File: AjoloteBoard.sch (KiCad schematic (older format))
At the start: 4 parts, among them SW1 SW_Push_SPDT

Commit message: Update project to kicad 5
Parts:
- removed SW1: SW_Push_SPDT, Switches:MSK12C02, symbol SW_Push_SPDT
- added SW?: SW_DPDT_x2, symbol Switch:SW_DPDT_x2
- BT1: symbol Battery_Cell -> Device:Battery_Cell
- D1, D2: symbol LED -> Device:LED
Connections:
- wire segments 9 -> 11
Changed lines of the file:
@@
-EESchema Schematic File Version 2
-LIBS:power
-LIBS:device
-LIBS:transistors
-LIBS:conn
-LIBS:linear
-LIBS:regul
-LIBS:74xx
-LIBS:cmos4000
-LIBS:adc-dac
-LIBS:memory
-LIBS:xilinx
-LIBS:microcontrollers
-LIBS:dsp
-LIBS:microchip
-LIBS:analog_switches
-LIBS:motorola
-LIBS:texas
-LIBS:intel
-LIBS:audio
-LIBS:interface
-LIBS:digital-audio
-LIBS:philips
-LIBS:display
-LIBS:cypress
-LIBS:siliconi
-LIBS:opto
-LIBS:atmel
-LIBS:contrib
-LIBS:valves
-LIBS:74xgxx
-LIBS:ac-dc
-LIBS:actel
-LIBS:allegro
-LIBS:Altera
-LIBS:analog_devices
-LIBS:battery_management
-LIBS:bbd
-LIBS:bosch
-LIBS:brooktre
-LIBS:cmos_ieee
-LIBS:dc-dc
-LIBS:diode
-LIBS:elec-unifil
-LIBS:ESD_Protection
-LIBS:ftdi
-LIBS:gennum
-LIBS:graphic
-LIBS:hc11
-LIBS:ir
-LIBS:Lattice
-LIBS:logo
-LIBS:maxim
-LIBS:mechanical
-LIBS:microchip_dspic33dsc
-LIBS:microchip_pic10mcu
-LIBS:microchip_pic12mcu
-LIBS:microchip_pic16mcu
-LIBS:microchip_pic18mcu
-LIBS:microchip_pic32mcu
-LIBS:motor_drivers
-LIBS:motors
-LIBS:msp430
-LIBS:nordicsemi
-LIBS:nxp_armmcu
-LIBS:onsemi
-LIBS:Oscillators
-LIBS:Power_Management
-LIBS:powerint
-LIBS:pspice
-LIBS:references
-LIBS:relays
-LIBS:rfcom
-LIBS:sensors
-LIBS:silabs
-LIBS:stm8
-LIBS:stm32
-LIBS:supertex
-LIBS:switches
-LIBS:transf
-LIBS:ttl_ieee
-LIBS:video
-LIBS:wiznet
-LIBS:Worldsemi
-LIBS:Xicor
-LIBS:zetex
-LIBS:Zilog
+EESchema Schematic File Version 4
 LIBS:AjoloteBoard-cache
-EELAYER 25 0
+EELAYER 29 0
 EELAYER END
 $Descr A4 11693 8268
@@
 $EndDescr
 $Comp
-L LED D1
+L Device:LED D1
 U 1 1 5AF7924C
 P 4745 3090
@@
 $EndComp
 $Comp
-L LED D2
+L Device:LED D2
 U 1 1 5AF7929C
 P 5100 3120
@@
 $EndComp
 $Comp
-L Battery_Cell BT1
+L Device:Battery_Cell BT1
 U 1 1 5AF792E6
 P 3895 3190
@@
 	1    0    0    -1
 $EndComp
-$Comp
-L SW_Push_SPDT SW1
-U 1 1 5B1026CD
-P 4335 3375
-F 0 "SW1" H 4335 3545 50  0000 C CNN
-F 1 "SW_Push_SPDT" H 4335 3175 50  0000 C CNN
-F 2 "Switches:MSK12C02" H 4335 3375 50  0001 C CNN
-F 3 "" H 4335 3375 50  0000 C CNN
-	1    4335 3375
-	1    0    0    -1
-$EndComp
 Wire Wire Line
 	3895 2990 3895 2890
 Wire Wire Line
-	3895 2890 5100 2890
+	3895 2890 4745 2890
 Wire Wire Line
 	3895 3290 3895 3375
@@
 	3895 3375 4135 3375
 Wire Wire Line
-	4535 3475 5100 3475
+	4535 3475 4745 3475
 Wire Wire Line
 	4745 3475 4745 3240
@@
 Connection ~ 4745 3475
 NoConn ~ 4535 3275
+Wire Wire Line
+	4745 2890 5100 2890
+Wire Wire Line
+	4745 3475 5100 3475
+$Comp
+L Switch:SW_DPDT_x2 SW?
+U 1 1 5DA6141C
+P 4335 3375
+F 0 "SW?" H 4335 3660 50  0000 C CNN
+F 1 "SW_DPDT_x2" H 4335 3569 50  0000 C CNN
+F 2 "" H 4335 3375 50  0001 C CNN
+F 3 "~" H 4335 3375 50  0001 C CNN
+	1    4335 3375
+	1    0    0    -1
+$EndComp
 $EndSCHEMATC

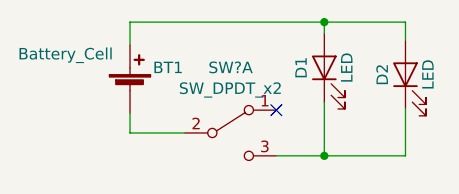
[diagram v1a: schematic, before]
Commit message: Update foorprints and floor plan
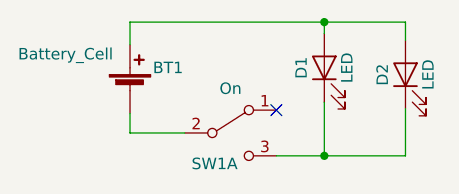
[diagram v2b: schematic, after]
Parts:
- BT1: footprint Batteries:BAT-HLD-012-SMT-OTL -> footprints:79523141
- D1, D2: footprint LEDs:LED_D5.0mm -> LED_THT:LED_D5.0mm_Clear
- SW1: renamed from SW?; value SW_DPDT_x2 -> On; footprint (none) -> footprints:Micro_interruptor_SPDT
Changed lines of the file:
@@
 F 0 "D1" H 4745 3190 50  0000 C CNN
 F 1 "LED" H 4745 2990 50  0000 C CNN
-F 2 "LEDs:LED_D5.0mm" H 4745 3090 50  0001 C CNN
+F 2 "LED_THT:LED_D5.0mm_Clear" H 4745 3090 50  0001 C CNN
 F 3 "" H 4745 3090 50  0000 C CNN
 	1    4745 3090
@@
 F 0 "D2" H 5100 3220 50  0000 C CNN
 F 1 "LED" H 5100 3020 50  0000 C CNN
-F 2 "LEDs:LED_D5.0mm" H 5100 3120 50  0001 C CNN
+F 2 "LED_THT:LED_D5.0mm_Clear" H 5100 3120 50  0001 C CNN
 F 3 "" H 5100 3120 50  0000 C CNN
 	1    5100 3120
@@
 F 0 "BT1" H 3995 3290 50  0000 L CNN
 F 1 "Battery_Cell" H 3405 3350 50  0000 L CNN
-F 2 "Batteries:BAT-HLD-012-SMT-OTL" V 3895 3250 50  0001 C CNN
+F 2 "footprints:79523141" V 3895 3250 50  0001 C CNN
 F 3 "" V 3895 3250 50  0000 C CNN
 	1    3895 3190
@@
 	4745 3475 5100 3475
 $Comp
-L Switch:SW_DPDT_x2 SW?
+L Switch:SW_DPDT_x2 SW1
 U 1 1 5DA6141C
 P 4335 3375
-F 0 "SW?" H 4335 3660 50  0000 C CNN
-F 1 "SW_DPDT_x2" H 4335 3569 50  0000 C CNN
-F 2 "" H 4335 3375 50  0001 C CNN
+F 0 "SW1" H 4265 3240 50  0000 C CNN
+F 1 "On" H 4335 3569 50  0000 C CNN
+F 2 "footprints:Micro_interruptor_SPDT" H 4335 3375 50  0001 C CNN
 F 3 "~" H 4335 3375 50  0001 C CNN
 	1    4335 3375
